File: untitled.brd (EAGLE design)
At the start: 50 x 50 mm, 68 parts, among them J1 5V, J2 R1171S421B-E2-FE, Q1 2N7002KW, Q10 2N7002KW, Q11 BSS138LT3G, Q2 2N7002KW, Q8 DMP2035U-7, Q9 2N7002KW, SW1 B3U-1000P-2P-SMD, SW2 B3U-1000P-2P-SMD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

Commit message: ver1.0
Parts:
- added C23: 10uf, Seeed-Capacitor:C0603
- added SW4: B3U-1000P-2P-SMD, Seeed-Switch:SW2-2.6-3.0X2.5X1.2+0.4MM
- added U$31: 10K, Seeed-Resistor:R0402
- moved TP8 10.2 mm to (18.5, 28.1)
- moved C1 5.12 mm to (23.3, 27.9), turned to 0 degrees
- moved C5 3.72 mm to (9.73, 42.9), turned to 270 degrees
- moved SW2 3.04 mm to (10.5, 46.5), turned to 90 degrees
- moved C4 2.55 mm to (13.8, 42.9), turned to 270 degrees
- moved C3 2.50 mm to (47.1, 47.7)
- moved C19 2.12 mm to (26.0, 31.5)
- moved SW1 1.58 mm to (14.5, 46.5), turned to 270 degrees
- moved C11 1.57 mm to (29.4, 8.96), turned to 0 degrees
- moved SW3 1.50 mm to (10.0, 46.5)
- moved U3 1.50 mm to (21.0, 33.5)
- moved C18 1.47 mm to (41.8, 47.7), turned to 180 degrees
- moved C21 1.41 mm to (14.4, 22.0), turned to 0 degrees
- moved C12 1.04 mm to (12.8, 28.7), turned to 0 degrees
- moved J1 1.00 mm to (4.62, 8.72)
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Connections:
- removed net ANT_POWR: U2.31
- new net TRAP_FORCE: C23.1, SW4.1, U$31.2, U2.7
- net GND: now also C23.2, U$31.1
- net PWRKEY: no longer JP1.13
- net RESET_N: no longer JP1.12
- net RXD_MODULE: now also U9.4; no longer U9.5
- net RX_MODULE2: now also JP1.4, U9.17; no longer JP1.5, U9.16
- net TXD_MODULE: now also U9.5; no longer U9.4
- net TX_MODULE2: now also JP1.5, U9.16; no longer JP1.4, U9.17
- net VDD_1V8: no longer JP1.11
- net VDD_3V3: now also SW4.2; no longer JP1.10
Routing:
- net PWRKEY_MODULE: track 1.26 -> 88.8 mm, vias 0 -> 6
- net USIM_VDD: track 7.40 -> 57.0 mm, vias 0 -> 2
- net TRAP_FORCE: track 0.00 -> 41.8 mm, vias 0 -> 2
- net M_POWER: track 0.00 -> 35.4 mm, vias 0 -> 2
- net TXD_MODULE: track 0.00 -> 29.5 mm, vias 0 -> 1
- net VDD_3V3: track 78.6 -> 105.6 mm
- net DTR: track 0.00 -> 23.9 mm, vias 0 -> 1
- net RXD_MODULE: track 0.00 -> 20.7 mm, vias 0 -> 1
- net RESET_N: track 0.00 -> 13.6 mm, vias 0 -> 1
- net PWRKEY: track 37.1 -> 48.3 mm, vias 0 -> 2
- net VDD_EXT: track 0.00 -> 10.1 mm, vias 0 -> 1
- net BOOTMODE: track 47.3 -> 38.2 mm
- net GND: track 0.00 -> 6.39 mm, vias 0 -> 8
- net VDD_1V8: track 7.67 -> 13.6 mm, vias 0 -> 2
- net NET_MODE: track 33.5 -> 36.6 mm, vias 1 -> 3
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- added copper zone on layer 1, net GND
- added copper zone on layer 16, net GND

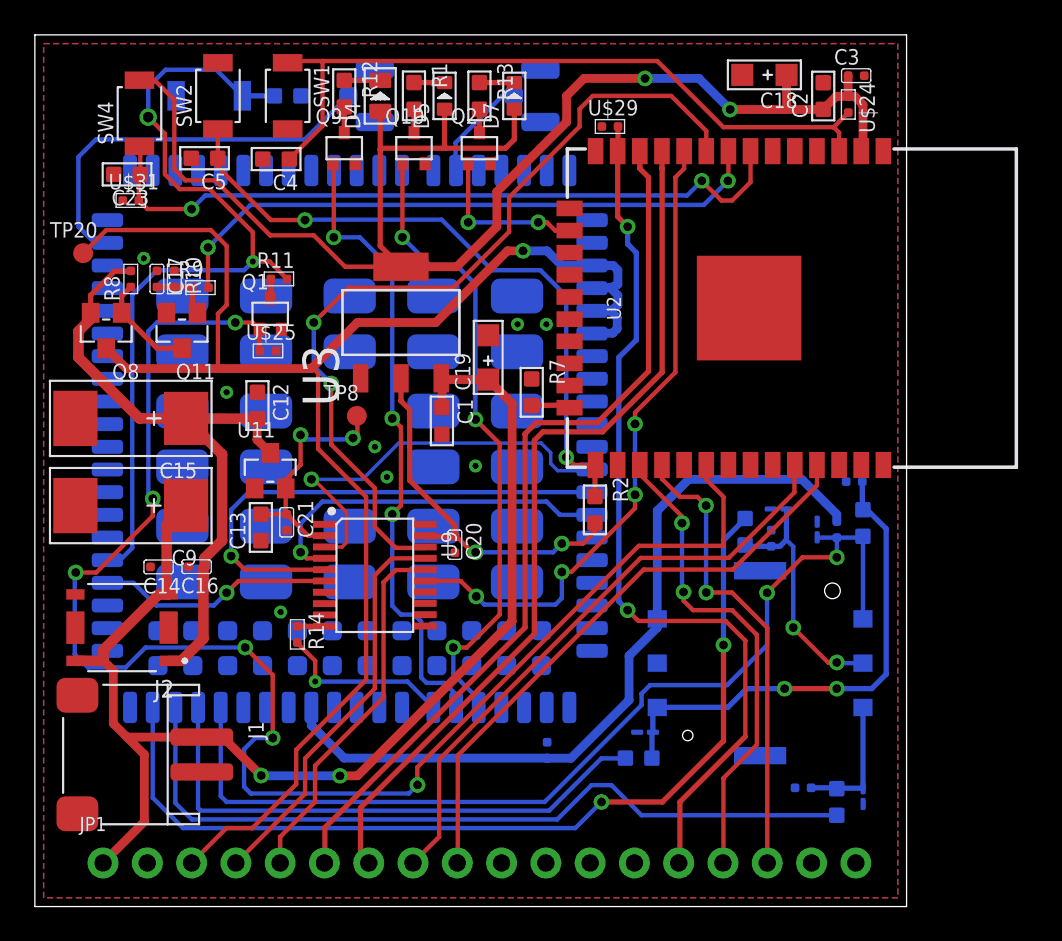
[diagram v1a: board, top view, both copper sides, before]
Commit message: MOSをSeeedのものに変更
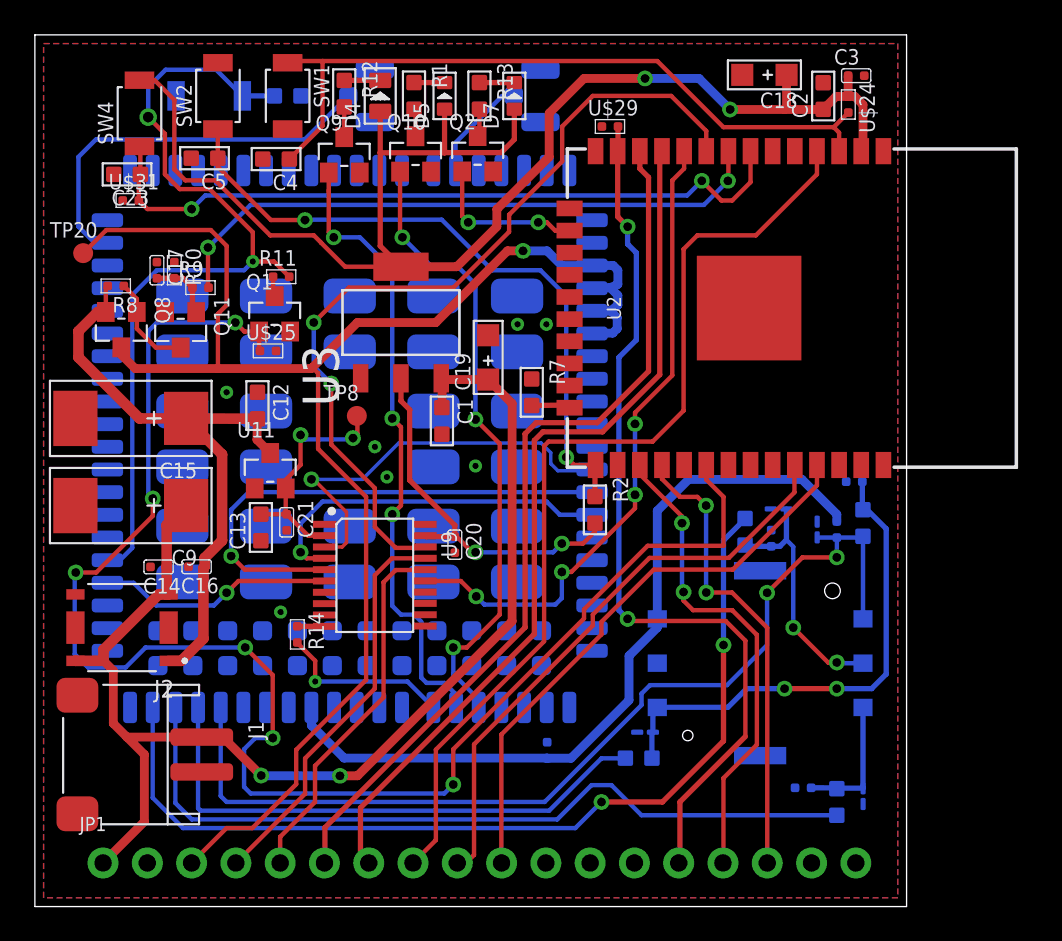
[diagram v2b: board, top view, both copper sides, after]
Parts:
- Q1, Q10, Q2, Q9: value 2N7002KW -> BSS138W-7-F; device Discrete-new:SOT-323 -> Seeed-Transistor:SOT-23
- Q11: value BSS138LT3G -> CJ2302; device Discrete-new:SOT-23 -> Seeed-Transistor:SOT-23
- Q8: value DMP2035U-7 -> NCE3407A; device Discrete-new:SOT-23 -> Seeed-Transistor:SOT-23
- moved R8 0.95 mm to (4.64, 35.6), turned to 270 degrees
- moved Q8 0.87 mm to (4.96, 33.1), turned to 180 degrees
- moved C17 0.50 mm to (7.00, 36.5)
- moved R10 0.50 mm to (8.00, 36.5)
- moved Q9 0.38 mm to (17.7, 43.1)
- moved Q10 0.34 mm to (21.8, 43.2)
- moved Q2 0.34 mm to (25.4, 43.2)
- moved Q1 0.25 mm to (13.8, 34.0)
- moved R11 0.18 mm to (14.1, 36.1)
- moved Q11 0.09 mm to (8.36, 33.1), turned to 180 degrees
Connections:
- net BATTERY_CHECK: now also JP1.8
- net RX_ESP: now also JP1.9; no longer JP1.8
- net TX_ESP: now also JP1.10; no longer JP1.9
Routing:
- net BATTERY_CHECK: track 0.00 -> 55.9 mm
- net VSYS: track 37.2 -> 35.5 mm
- net TX_ESP: track 34.4 -> 33.0 mm
- net RX_ESP: track 34.9 -> 33.8 mm
- net PWRKEY_MODULE: track 88.8 -> 89.6 mm
- net VBAT: track 92.0 -> 91.4 mm
- net GND: track 6.39 -> 6.59 mm, vias 8 -> 7
